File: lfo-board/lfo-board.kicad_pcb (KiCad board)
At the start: 2 copper layers, 22.9 x 68.6 mm, 4 parts

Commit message: Before removing attenuverters
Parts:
- added C1: 10n, Capacitor_SMD:C_0603_1608Metric_Pad1.08x0.95mm_HandSolder, F.Cu at (175.6, 51.7)
- added C10: 100n, Capacitor_SMD:C_0603_1608Metric_Pad1.08x0.95mm_HandSolder, F.Cu at (162.6, 55.6)
- added C11: 100n, Capacitor_SMD:C_0603_1608Metric_Pad1.08x0.95mm_HandSolder, F.Cu at (164.8, 60.7)
- added C12: 10u, Capacitor_Tantalum_SMD:CP_EIA-3216-10_Kemet-I_Pad1.58x1.35mm_HandSolder, F.Cu at (38.6, 53.8)
- added C13: 330n, Capacitor_Tantalum_SMD:CP_EIA-3216-10_Kemet-I_Pad1.58x1.35mm_HandSolder, F.Cu at (35.3, 53.8)
- added C14: 100n, Capacitor_SMD:C_0603_1608Metric_Pad1.08x0.95mm_HandSolder, F.Cu at (33.8, 83.1)
- added C15: 100n, Capacitor_Tantalum_SMD:CP_EIA-3216-10_Kemet-I_Pad1.58x1.35mm_HandSolder, F.Cu at (38.6, 59.7)
- added C16: 10u, Capacitor_Tantalum_SMD:CP_EIA-3216-10_Kemet-I_Pad1.58x1.35mm_HandSolder, F.Cu at (42.2, 59.6)
- added C17: 10n, Capacitor_SMD:C_0603_1608Metric_Pad1.08x0.95mm_HandSolder, F.Cu at (37.2, 78.9)
- added C18: 4.7n, Capacitor_SMD:C_0603_1608Metric_Pad1.08x0.95mm_HandSolder, F.Cu at (41.9, 73.0)
- added C19: 100n, Capacitor_SMD:C_0603_1608Metric_Pad1.08x0.95mm_HandSolder, F.Cu at (32.3, 67.7)
- added C2: 10n, Capacitor_SMD:C_0603_1608Metric_Pad1.08x0.95mm_HandSolder, F.Cu at (175.6, 54.2)
- added C3: 10n, Capacitor_SMD:C_0603_1608Metric_Pad1.08x0.95mm_HandSolder, F.Cu at (160.4, 62.6)
- added C4: 10n, Capacitor_SMD:C_0603_1608Metric_Pad1.08x0.95mm_HandSolder, F.Cu at (170.7, 58.1)
- added C5: 10n, Capacitor_SMD:C_0603_1608Metric_Pad1.08x0.95mm_HandSolder, F.Cu at (146.0, 74.3)
- added C6: 10n, Capacitor_SMD:C_0603_1608Metric_Pad1.08x0.95mm_HandSolder, F.Cu at (162.0, 58.1)
- added C7: 10n, Capacitor_SMD:C_0603_1608Metric_Pad1.08x0.95mm_HandSolder, F.Cu at (154.7, 75.4)
- added C8: 10n, Capacitor_SMD:C_0603_1608Metric_Pad1.08x0.95mm_HandSolder, F.Cu at (178.9, 46.7)
- added C9: 100n, Capacitor_SMD:C_0603_1608Metric_Pad1.08x0.95mm_HandSolder, F.Cu at (156.1, 63.3)
- added D1: 4001, Diode_SMD:D_SMA_Handsoldering, F.Cu at (148.9, 64.3)
- added D2: LED_Dual_Bidirectional, LED_SMD:LED_0603_1608Metric_Pad1.05x0.95mm_HandSolder, F.Cu at (37.1, 64.4)
- added J1: Conn_01x25, Connector_PinSocket_2.54mm:PinSocket_1x25_P2.54mm_Vertical, F.Cu at (45.7, 58.4)
- added J2: Conn_01x25, Connector_PinSocket_2.54mm:PinSocket_1x25_P2.54mm_Vertical, F.Cu at (27.9, 58.4)
- added Q1: MMBT3904, Package_TO_SOT_SMD:SOT-23, F.Cu at (157.9, 54.1)
- added R1: 100K, Resistor_SMD:R_0603_1608Metric_Pad0.98x0.95mm_HandSolder, F.Cu at (146.0, 79.3)
- added R10: 100K, Resistor_SMD:R_0603_1608Metric_Pad0.98x0.95mm_HandSolder, F.Cu at (31.6, 94.9)
- added R11: 100K, Resistor_SMD:R_0603_1608Metric_Pad0.98x0.95mm_HandSolder, F.Cu at (31.6, 98.7)
- added R12: 100K, Resistor_SMD:R_0603_1608Metric_Pad0.98x0.95mm_HandSolder, F.Cu at (174.6, 49.2)
- added R13: 100K, Resistor_SMD:R_0603_1608Metric_Pad0.98x0.95mm_HandSolder, F.Cu at (146.0, 81.9)
- added R14: 1K, Resistor_SMD:R_0603_1608Metric_Pad0.98x0.95mm_HandSolder, F.Cu at (159.1, 70.9)
- added R15: 1K, Resistor_SMD:R_0603_1608Metric_Pad0.98x0.95mm_HandSolder, F.Cu at (162.6, 53.1)
- added R16: 100K, Resistor_SMD:R_0603_1608Metric_Pad0.98x0.95mm_HandSolder, F.Cu at (163.2, 68.2)
- added R17: 100K, Resistor_SMD:R_0603_1608Metric_Pad0.98x0.95mm_HandSolder, F.Cu at (150.4, 74.3)
- added R18: 100K, Resistor_SMD:R_0603_1608Metric_Pad0.98x0.95mm_HandSolder, F.Cu at (178.9, 49.2)
- added R19: 100K, Resistor_SMD:R_0603_1608Metric_Pad0.98x0.95mm_HandSolder, F.Cu at (154.5, 70.4)
- added R2: 100K, Resistor_SMD:R_0603_1608Metric_Pad0.98x0.95mm_HandSolder, F.Cu at (164.8, 63.2)
- added R20: 220K, Resistor_SMD:R_0603_1608Metric_Pad0.98x0.95mm_HandSolder, F.Cu at (163.2, 65.7)
- added R21: 100K, Resistor_SMD:R_0603_1608Metric_Pad0.98x0.95mm_HandSolder, F.Cu at (166.9, 53.1)
- added R22: 100K, Resistor_SMD:R_0603_1608Metric_Pad0.98x0.95mm_HandSolder, F.Cu at (158.8, 65.8)
- added R23: 220K, Resistor_SMD:R_0603_1608Metric_Pad0.98x0.95mm_HandSolder, F.Cu at (154.5, 67.9)
- added R24: 100K, Resistor_SMD:R_0603_1608Metric_Pad0.98x0.95mm_HandSolder, F.Cu at (154.7, 72.9)
- added R25: 100K, Resistor_SMD:R_0603_1608Metric_Pad0.98x0.95mm_HandSolder, F.Cu at (169.1, 60.7)
- added R26: 100K, Resistor_SMD:R_0603_1608Metric_Pad0.98x0.95mm_HandSolder, F.Cu at (157.7, 57.6)
- added R27: 100K, Resistor_SMD:R_0603_1608Metric_Pad0.98x0.95mm_HandSolder, F.Cu at (157.7, 60.1)
- added R28: 1K, Resistor_SMD:R_0603_1608Metric_Pad0.98x0.95mm_HandSolder, F.Cu at (166.9, 55.6)
- added R29: 1K, Resistor_SMD:R_0603_1608Metric_Pad0.98x0.95mm_HandSolder, F.Cu at (146.0, 84.4)
- added R3: 100K, Resistor_SMD:R_0603_1608Metric_Pad0.98x0.95mm_HandSolder, F.Cu at (150.4, 79.3)
- added R30: 330K, Resistor_SMD:R_0603_1608Metric_Pad0.98x0.95mm_HandSolder, F.Cu at (32.3, 78.9)
- added R31: 75K, Resistor_SMD:R_0603_1608Metric_Pad0.98x0.95mm_HandSolder, F.Cu at (41.9, 78.7)
- added R32: 20K, Resistor_SMD:R_0603_1608Metric_Pad0.98x0.95mm_HandSolder, F.Cu at (41.9, 75.8)
- added R33: 100K, Resistor_SMD:R_0603_1608Metric_Pad0.98x0.95mm_HandSolder, F.Cu at (32.3, 71.6)
- added R34: 470, Resistor_SMD:R_0603_1608Metric_Pad0.98x0.95mm_HandSolder, F.Cu at (41.9, 64.4)
- added R35: 20K, Resistor_SMD:R_0603_1608Metric_Pad0.98x0.95mm_HandSolder, F.Cu at (32.3, 64.4)
- added R36: 24K, Resistor_SMD:R_0603_1608Metric_Pad0.98x0.95mm_HandSolder, F.Cu at (32.3, 75.8)
- added R37: 100K, Resistor_SMD:R_0603_1608Metric_Pad0.98x0.95mm_HandSolder, F.Cu at (37.1, 75.8)
- added R38: 1K, Resistor_SMD:R_0603_1608Metric_Pad0.98x0.95mm_HandSolder, F.Cu at (41.9, 69.0)
- added R4: 100K, Resistor_SMD:R_0603_1608Metric_Pad0.98x0.95mm_HandSolder, F.Cu at (174.6, 46.7)
- added R5: 10K, Resistor_SMD:R_0603_1608Metric_Pad0.98x0.95mm_HandSolder, F.Cu at (166.4, 58.1)
- added R6: 220K, Resistor_SMD:R_0603_1608Metric_Pad0.98x0.95mm_HandSolder, F.Cu at (158.8, 68.3)
- added R7: 100K, Resistor_SMD:R_0603_1608Metric_Pad0.98x0.95mm_HandSolder, F.Cu at (150.4, 76.8)
- added R8: 100K, Resistor_SMD:R_0603_1608Metric_Pad0.98x0.95mm_HandSolder, F.Cu at (43.1, 99.7)
- added R9: 220K, Resistor_SMD:R_0603_1608Metric_Pad0.98x0.95mm_HandSolder, F.Cu at (171.2, 53.1)
- added SW1: SW_Push, Button_Switch_SMD:SW_Push_SPST_NO_Alps_SKRK, F.Cu at (143.4, 46.8)
- added U1: OPA4991, Package_SO:SOIC-14_3.9x8.7mm_P1.27mm, F.Cu at (37.2, 106.3)
- added U2: MCP6002, Package_SO:SOIC-8_3.9x4.9mm_P1.27mm, F.Cu at (37.3, 98.4)
- added U3: MCP6002, Package_SO:SOIC-8_3.9x4.9mm_P1.27mm, F.Cu at (168.2, 48.6)
- added U4: StompLFO, Package_SO:SOIC-8_3.9x4.9mm_P1.27mm, F.Cu at (37.1, 87.1)
- added U5: L78L05, Package_TO_SOT_SMD:SOT-89-3, F.Cu at (33.0, 59.9)
- added U6: TL972, Package_SO:SOIC-8_3.9x4.9mm_P1.27mm, F.Cu at (37.1, 71.0)
- moved H101 31.8 mm to (43.2, 124.5)
- moved H103 31.8 mm to (30.5, 124.5)
- moved H102 28.0 mm to (30.5, 53.4)
- moved H104 28.0 mm to (43.2, 53.4)
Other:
- board size 22.9 x 68.6 mm -> 22.9 x 81.3 mm
- copper layers 2 -> 4

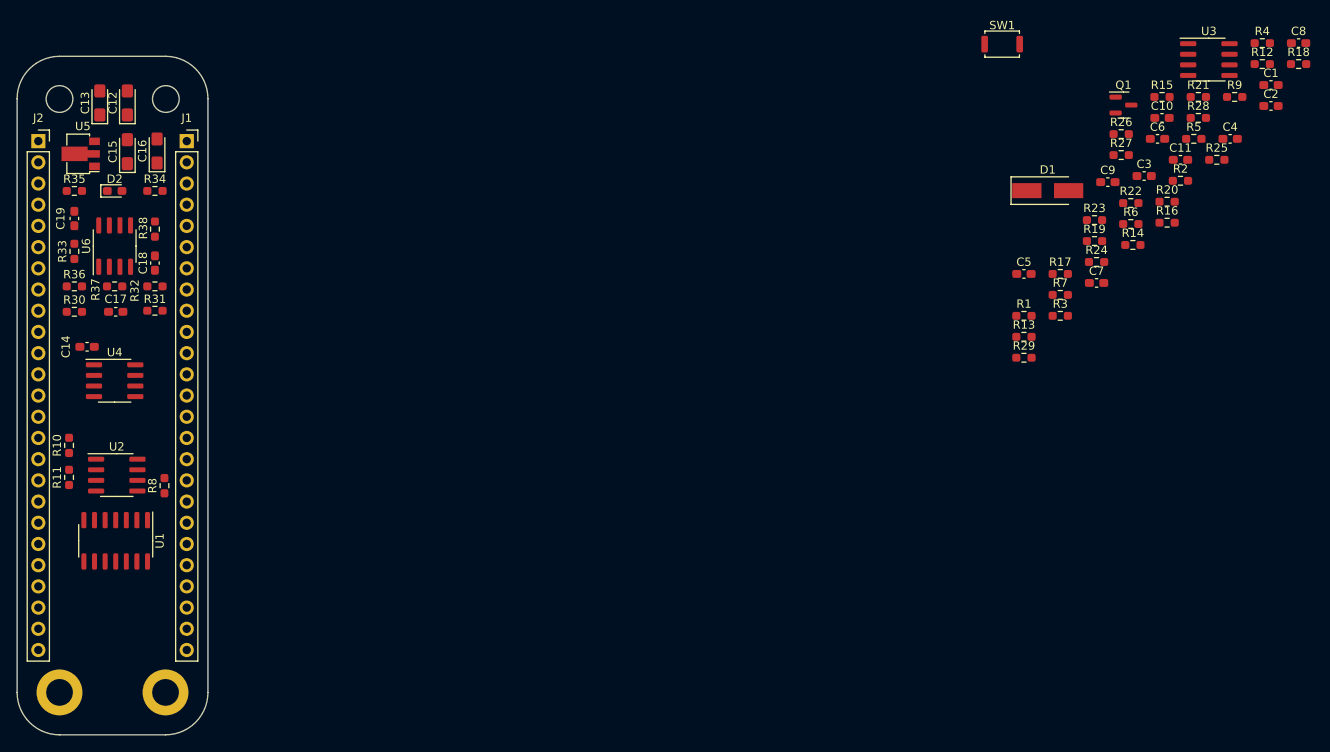
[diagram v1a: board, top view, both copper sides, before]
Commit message: LFO graphics
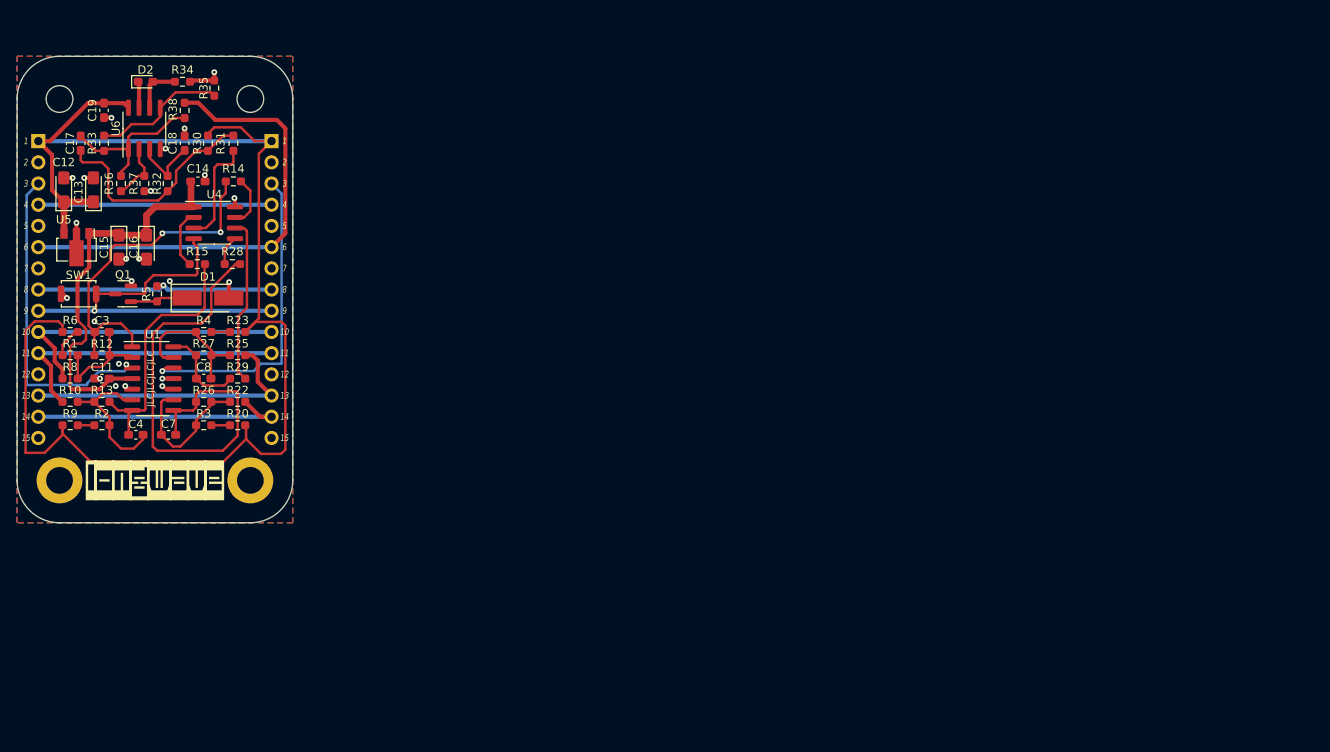
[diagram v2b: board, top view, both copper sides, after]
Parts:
- removed C1, C2, C5, C6: 10n, Capacitor_SMD:C_0603_1608Metric_Pad1.08x0.95mm_HandSolder
- removed C10, C9: 100n, Capacitor_SMD:C_0603_1608Metric_Pad1.08x0.95mm_HandSolder
- removed H101, H103: GND, MountingHole:MountingHole_3.2mm_M3_ISO14580_Pad
- removed R11, R16, R17, R18, R19, R21, R24, R7: 100K, Resistor_SMD:R_0603_1608Metric_Pad0.98x0.95mm_HandSolder
- removed U2, U3: MCP6002, Package_SO:SOIC-8_3.9x4.9mm_P1.27mm
- added G***: LOGO, LOGO, B.Cu at (41.9, 99.1)
- added H1: GND, MountingHole:MountingHole_3.2mm_M3_ISO14580_Pad, F.Cu at (30.5, 99.1)
- added H3: GND, MountingHole:MountingHole_3.2mm_M3_ISO14580_Pad, F.Cu at (53.3, 99.1)
- added REF**: OSHW-Logo2_7.3x6mm_SilkScreen, Symbol:OSHW-Logo2_7.3x6mm_SilkScreen, B.Cu at (41.9, 53.3)
- added kibuzzard-65FC58C1: G***, kibuzzard-65FC58C1, B.Cu at (31.8, 58.4)
- added kibuzzard-65FC5928: G***, kibuzzard-65FC5928, B.Cu at (31.8, 68.6)
- added kibuzzard-65FC5928: G***, kibuzzard-65FC5928, B.Cu at (31.8, 94.0)
- added kibuzzard-65FC5928: G***, kibuzzard-65FC5928, B.Cu at (31.8, 61.0)
- added kibuzzard-65FC5928: G***, kibuzzard-65FC5928, B.Cu at (31.8, 73.7)
- added kibuzzard-65FC5928: G***, kibuzzard-65FC5928, B.Cu at (31.8, 86.4)
- added kibuzzard-65FC593A: G***, kibuzzard-65FC593A, B.Cu at (31.8, 63.5)
- added kibuzzard-65FC5990: G***, kibuzzard-65FC5990, B.Cu at (31.8, 76.2)
- added kibuzzard-65FC599C: G***, kibuzzard-65FC599C, B.Cu at (31.8, 78.7)
- added kibuzzard-65FC59AA: G***, kibuzzard-65FC59AA, B.Cu at (31.8, 81.3)
- added kibuzzard-65FC59B5: G***, kibuzzard-65FC59B5, B.Cu at (31.8, 83.8)
- added kibuzzard-65FC59D5: G***, kibuzzard-65FC59D5, B.Cu at (31.8, 88.9)
- added kibuzzard-65FC59E3: G***, kibuzzard-65FC59E3, B.Cu at (31.8, 91.4)
- added kibuzzard-65FC59FD: G***, kibuzzard-65FC59FD, B.Cu at (31.8, 66.0)
- added kibuzzard-65FC5A15: G***, kibuzzard-65FC5A15, B.Cu at (31.8, 71.1)
- added kibuzzard-65FC5A8F: G***, kibuzzard-65FC5A8F, B.Cu at (52.1, 58.4)
- added kibuzzard-65FC5A9B: G***, kibuzzard-65FC5A9B, B.Cu at (52.1, 68.6)
- added kibuzzard-65FC5A9B: G***, kibuzzard-65FC5A9B, B.Cu at (52.1, 86.4)
- added kibuzzard-65FC5A9B: G***, kibuzzard-65FC5A9B, B.Cu at (52.1, 73.7)
- added kibuzzard-65FC5A9B: G***, kibuzzard-65FC5A9B, B.Cu at (52.1, 94.0)
- added kibuzzard-65FC5A9B: G***, kibuzzard-65FC5A9B, B.Cu at (52.1, 61.0)
- added kibuzzard-65FC5ACC: G***, kibuzzard-65FC5ACC, B.Cu at (52.1, 63.5)
- added kibuzzard-65FC5ADA: G***, kibuzzard-65FC5ADA, B.Cu at (52.1, 76.2)
- added kibuzzard-65FC5AE2: G***, kibuzzard-65FC5AE2, B.Cu at (52.1, 78.7)
- added kibuzzard-65FC5AF0: G***, kibuzzard-65FC5AF0, B.Cu at (52.1, 81.3)
- added kibuzzard-65FC5AF9: G***, kibuzzard-65FC5AF9, B.Cu at (52.1, 83.8)
- added kibuzzard-65FC5B08: G***, kibuzzard-65FC5B08, B.Cu at (52.1, 88.9)
- added kibuzzard-65FC5B16: G***, kibuzzard-65FC5B16, B.Cu at (52.1, 91.4)
- added kibuzzard-65FC5B2E: G***, kibuzzard-65FC5B2E, B.Cu at (52.1, 66.0)
- added kibuzzard-65FC5B39: G***, kibuzzard-65FC5B39, B.Cu at (52.1, 71.1)
- added kibuzzard-65FC6621: G***, kibuzzard-65FC6621, F.Cu at (41.9, 99.1)
- C17: value 10n -> 6.8n
- H2: renamed from H102; value 1 -> 2
- H4: renamed from H104; value 2 -> 1
- J1, J2: value Conn_01x25 -> Conn_01x15; footprint Connector_PinSocket_2.54mm:PinSocket_1x25_P2.54mm_Vertical -> Connector_PinSocket_2.54mm:PinSocket_1x15_P2.54mm_Vertical
- R1, R2, R3, R4: value 100K -> 4.7K
- U1: value OPA4991 -> MCP6004
- moved R9 144.9 mm to (31.8, 92.5)
- moved R12 143.3 mm to (35.6, 84.1), turned to 180 degrees
- moved C8 137.2 mm to (47.8, 86.9), turned to 180 degrees
- moved C4 135.8 mm to (39.6, 93.6), turned to 180 degrees
- moved R2 132.5 mm to (35.6, 92.5)
- moved C11 131.8 mm to (35.6, 86.9), turned to 180 degrees
- moved R4 131.4 mm to (47.8, 81.3), turned to 180 degrees
- moved R6 127.7 mm to (31.8, 81.3)
- moved C3 126.2 mm to (35.6, 81.3), turned to 180 degrees
- moved R5 125.6 mm to (42.2, 76.7), turned to -90 degrees
- moved Q1 121.9 mm to (38.1, 76.7), turned to 180 degrees
- moved R25 119.6 mm to (51.8, 84.1), turned to 180 degrees
- moved R15 117.3 mm to (47.0, 73.2), turned to 180 degrees
- moved R28 117.0 mm to (51.2, 73.2), turned to 180 degrees
- moved SW1 114.6 mm to (32.8, 76.7)
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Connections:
- J1 pad 10: /Offset1 -> /Vfreq
- J1 pad 11: /Offset2 -> /Vof
- J1 pad 12: /+4.5V -> /GND
- J1 pad 13: /GND -> /Vform
- J1 pad 14: /WForm1 -> /Vdepth
- J1 pad 15: /WForm2 -> /GND
- J1 pad 4: /Out -> /+5V
- J1 pad 6: /Freq1 -> /Out
- J1 pad 7: /Freq2 -> /GND
- J1 pad 8: /+4.5V -> /Sync
- J1 pad 9: /GND -> /Tap
- J2 pad 10: /Offset1 -> /Vfreq
- J2 pad 11: /Offset2 -> /Vof
- J2 pad 12: /+4.5V -> /GND
- J2 pad 13: /GND -> /Vform
- J2 pad 14: /WForm1 -> /Vdepth
- J2 pad 15: /WForm2 -> /GND
- J2 pad 4: /Out -> /+5V
- J2 pad 6: /Freq1 -> /Out
- J2 pad 7: /Freq2 -> /GND
- J2 pad 8: /+4.5V -> /Sync
- J2 pad 9: /GND -> /Tap
- R1 pad 1: /Offset1 -> Net-(R1-Pad1)
- R1 pad 2: Net-(C1-Pad1) -> Net-(C3-Pad1)
- R10 pad 1: /FreqOf -> /Vof
- R14 pad 2: /LFO/OffsetCV -> /LFO/FreqCV
- R15 pad 2: /LFO/FreqCV -> /LFO/OffsetCV
- R2 pad 1: /Freq1 -> Net-(R2-Pad1)
- R2 pad 2: Net-(C2-Pad1) -> Net-(C4-Pad1)
- R20 pad 2: Net-(C7-Pad1) -> Net-(R20-Pad2)
- R22 pad 1: Net-(C5-Pad2) -> /Vdepth
- R23 pad 2: Net-(C8-Pad1) -> Net-(R23-Pad2)
- R25 pad 1: Net-(C6-Pad2) -> /Vform
- R28 pad 2: /LFO/WaveformCV -> /LFO/DepthCV
- R29 pad 2: /LFO/DepthCV -> /LFO/WaveformCV
- R3 pad 1: Net-(C1-Pad1) -> Net-(R20-Pad2)
- R3 pad 2: Net-(C1-Pad2) -> Net-(C7-Pad1)
- R4 pad 1: Net-(C2-Pad1) -> Net-(R23-Pad2)
- R4 pad 2: Net-(C2-Pad2) -> Net-(C8-Pad1)
- R6 pad 2: Net-(C3-Pad1) -> Net-(R1-Pad1)
- R8 pad 1: Net-(C1-Pad2) -> /Vfreq
- R9 pad 2: Net-(C4-Pad1) -> Net-(R2-Pad1)
- U1 pad 1: Net-(C1-Pad2) -> Net-(C3-Pad2)
- U1 pad 10: /WForm2 -> /+4.5V
- U1 pad 12: /Depth2 -> /+4.5V
- U1 pad 13: Net-(C6-Pad1) -> Net-(C8-Pad1)
- U1 pad 14: Net-(C6-Pad2) -> Net-(C8-Pad2)
- U1 pad 2: Net-(C1-Pad1) -> Net-(C3-Pad1)
- U1 pad 3: /Offset2 -> /+4.5V
- U1 pad 4: /+9V -> /+5V
- U1 pad 5: /Freq2 -> /+4.5V
- U1 pad 6: Net-(C2-Pad1) -> Net-(C4-Pad1)
- U1 pad 7: Net-(C2-Pad2) -> Net-(C4-Pad2)
- U1 pad 8: Net-(C5-Pad2) -> Net-(C7-Pad2)
- U1 pad 9: Net-(C5-Pad1) -> Net-(C7-Pad1)
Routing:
- net /+9V: track 0.00 -> 169.9 mm
- net /+4.5V: track 0.00 -> 83.6 mm, vias 0 -> 5
- net /+5V: track 0.00 -> 75.6 mm
- net Net-(C7-Pad2): track 0.00 -> 58.2 mm
- net /Out: track 0.00 -> 56.2 mm
- net /Tap: track 0.00 -> 48.2 mm, vias 0 -> 1
- net Net-(C3-Pad2): track 0.00 -> 41.5 mm, vias 0 -> 2
- net /Vof: track 0.00 -> 35.0 mm
- net /Vfreq: track 0.00 -> 34.7 mm
- net /Vform: track 0.00 -> 34.6 mm
- net /Vdepth: track 0.00 -> 31.8 mm
- net Net-(C4-Pad2): track 0.00 -> 30.7 mm
- net /Sync: track 0.00 -> 29.2 mm, vias 0 -> 1
- net Net-(C17-Pad1): track 0.00 -> 27.4 mm
- net /LFO/WaveformCV: track 0.00 -> 20.0 mm
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- added copper zone on B.Cu, net /+4.5V
- added copper zone on F.Cu, net /+5V
- added copper zone on In1.Cu, net /GND
- added copper zone on In2.Cu, net /GND
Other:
- board size 22.9 x 81.3 mm -> 33 x 55.9 mm
- board text added: "1"
- board text added: "10"
- board text added: "11"
- board text added: "12"
- board text added: "13"
- board text added: "14"
- board text added: "15"
- board text added: "2"
- board text added: "3"
- board text added: "4"
- board text added: "5"
- board text added: "6"
- board text added: "7"
- board text added: "8"
- board text added: "9"
- board text added: "JLCJLCJLCJLC"
- board text added: "pedalmarkt.com"
- board text added: "v1rev1"

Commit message: wip attenuverters
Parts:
- D2: footprint LED_SMD:LED_0603_1608Metric_Pad1.05x0.95mm_HandSolder -> LED_THT:LED_D3.0mm
- moved D2 2.46 mm to (43.2, 50.8), turned to 180 degrees
- moved R35 1.28 mm to (49.1, 50.8)
- moved R34 1.25 mm to (46.4, 50.8), turned to 90 degrees
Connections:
- R34 pad 1: Net-(D2-Pad2) -> Net-(D2-Pad1)
- U6 pad 6: Net-(D2-Pad2) -> Net-(D2-Pad1)
- U6 pad 7: Net-(D2-Pad1) -> Net-(D2-Pad2)
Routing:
- net Net-(D2-Pad1): track 3.15 -> 7.96 mm
- net Net-(D2-Pad2): track 5.91 -> 3.89 mm
- net Net-(R33-Pad2): track 16.2 -> 16.8 mm

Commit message: Attvert graphics
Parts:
- moved REF** 2.54 mm to (41.9, 55.9)
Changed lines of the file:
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@@
   )
   (footprint "Symbol:OSHW-Logo2_7.3x6mm_SilkScreen" (layer "B.Cu")
-    (at 41.91 53.34 180)
+    (at 41.91 55.88 180)
     (descr "Open Source Hardware Symbol")
     (tags "Logo Symbol OSHW")

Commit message: LFO board jlc
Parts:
- C17: value 6.8n -> 10n
- R34: value 470 -> 1k
